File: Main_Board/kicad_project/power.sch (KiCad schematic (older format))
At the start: 32 parts

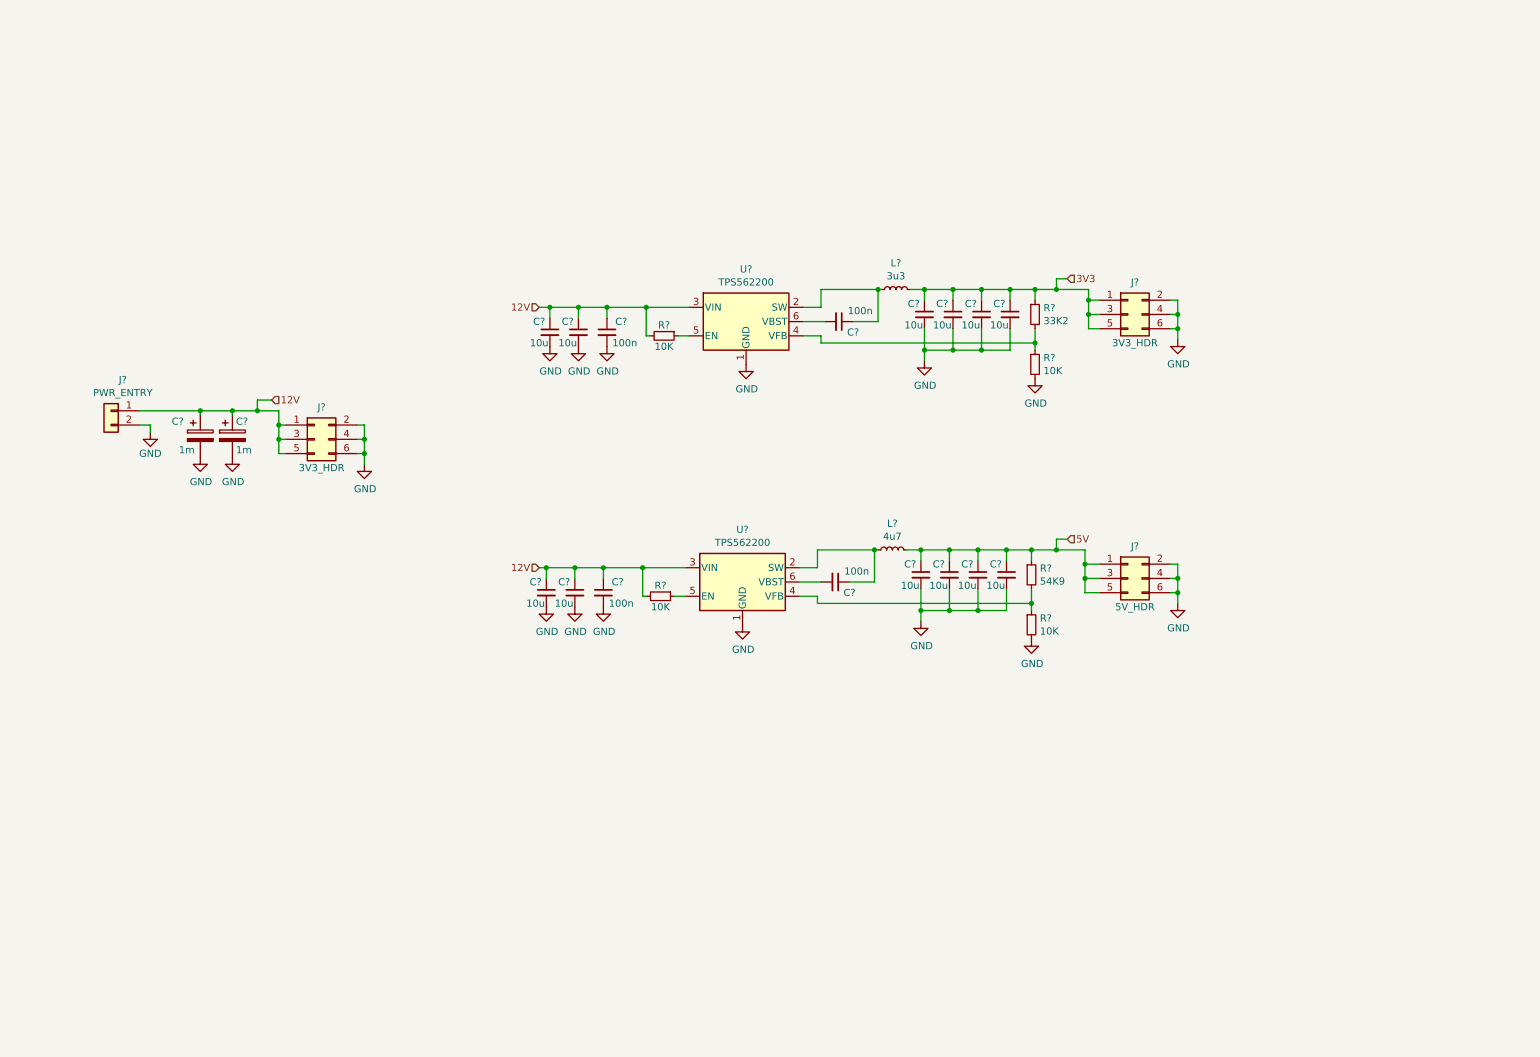
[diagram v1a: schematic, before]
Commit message: add input/output schematic, add documentation
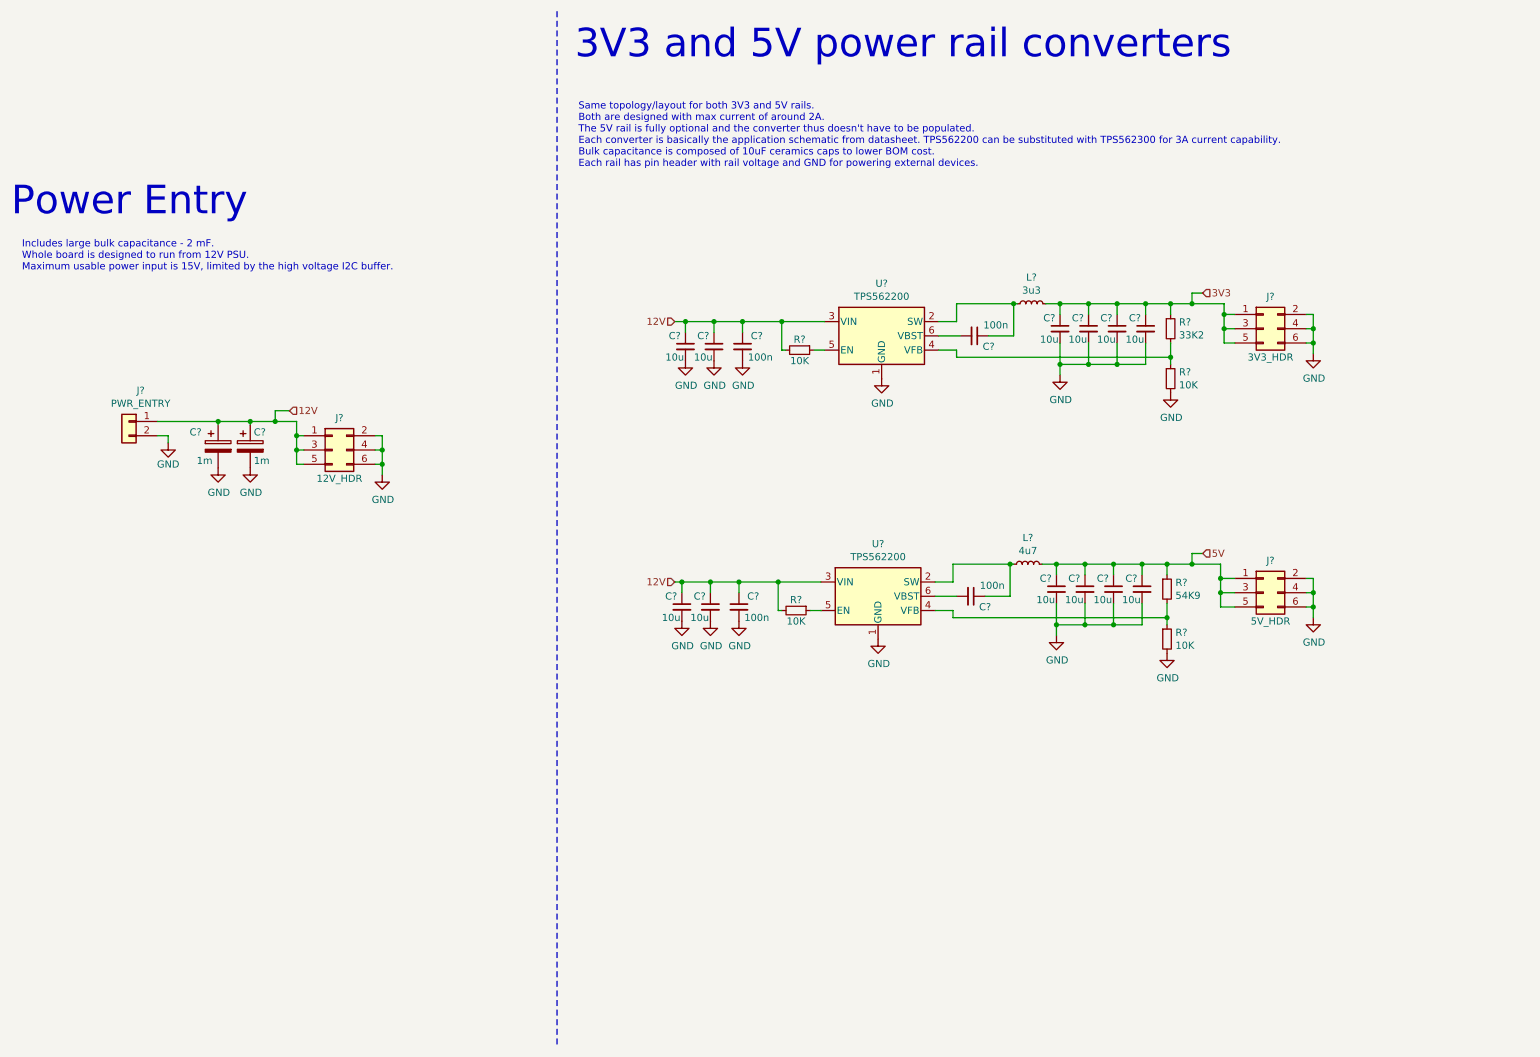
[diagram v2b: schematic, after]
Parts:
- J?: value 3V3_HDR -> 12V_HDR
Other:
- note added: "3V3 and 5V power rail converters"
- note added: "Includes large bulk capacitance - 2 mF.\nWhole board is designed to run from 12V PSU.\nMaximum usable power input is 15V, limited by the high voltage I2C buffer."
- note added: "Power Entry"
- note added: "Same topology/layout for both 3V3 and 5V rails.\nBoth are designed with max current of around 2A.\nThe 5V rail is fully optional and the converter thus doesn't have to be populated.\nEach converter is basically the application schematic from datasheet. TPS562200 can be substituted with TPS562300 for 3A current capability.\nBulk capacitance is composed of 10uF ceramics caps to lower BOM cost.\nEac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"
- moved on the sheet: C?, J?, L?, R?, U?

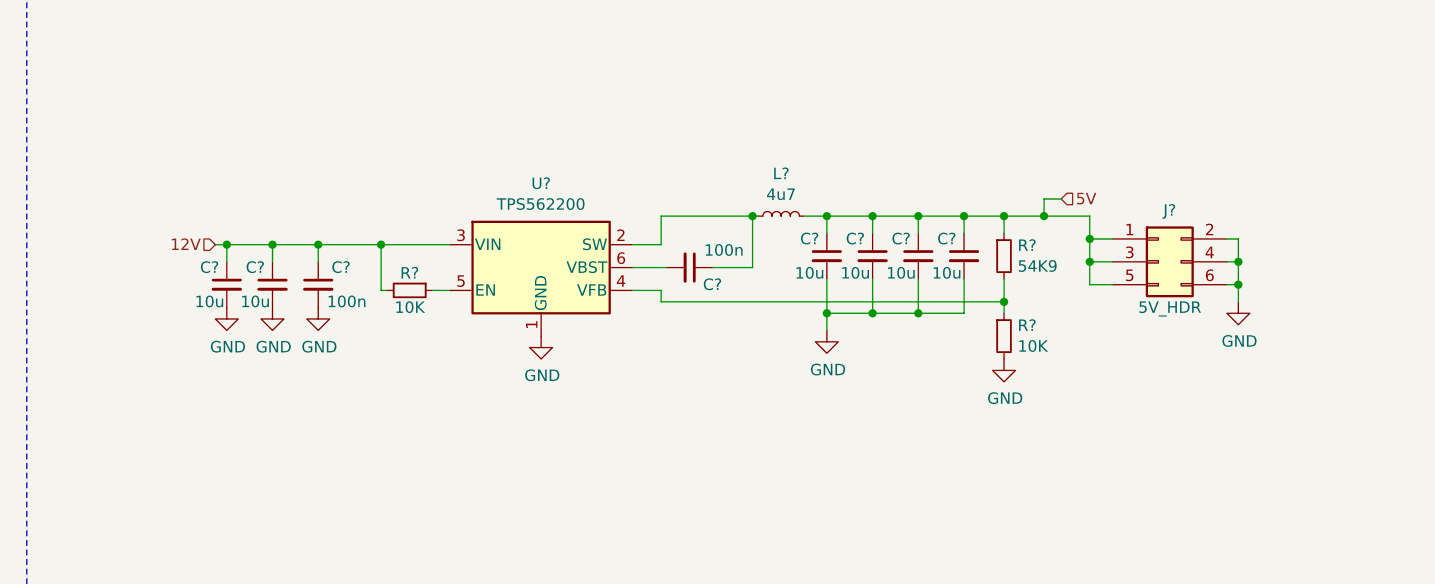
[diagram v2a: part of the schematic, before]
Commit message: add external IO
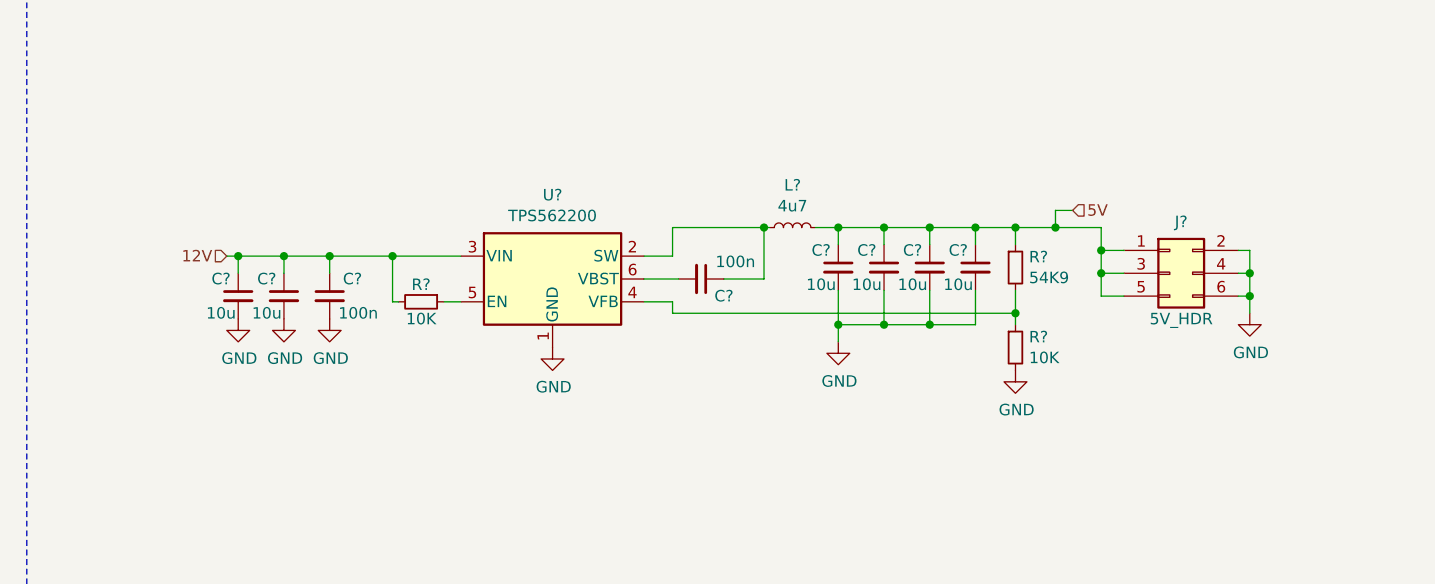
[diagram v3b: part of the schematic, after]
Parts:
- L? (x2): footprint (none) -> LoaDy:BOURNS_SRP3020TA
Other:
- moved on the sheet: C?, J?, L?, R?, U?

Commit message: schematic rev1 finished
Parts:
- gave numbers to parts that had none: 32
